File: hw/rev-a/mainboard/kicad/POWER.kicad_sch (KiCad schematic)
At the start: 66 parts, among them J10 5V PWR, J11 9V POWER, J13 9V POWER JACK, J27 6V POWER, J8 PET POWER, U3 AMS1117-3.3, U4 LM317AG-TN3-R, U5 LM317AG-TN3-R, U6 TPS5430DDA

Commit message: hw: use TLV1117LV instead of AMS1117
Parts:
- C89: value 15000u -> 120uF; MOUSER 661-BV250L153AM40S -> 667-EEU-FM1H121LB; now fitted
- R6, R8: value 1 -> 0; LCSC C22936 -> C21189
- U3: value AMS1117-3.3 -> TLV1117LV33; LCSC C6186 -> C15578
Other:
- note added: "*TLV1117LV33 substituted for AMS1117-3.3 due to incorrect placement of R6/R8 for ESR compensation"
- note added: "Configurable PS filtering caps"
- note removed: "Optional PS filtering caps. Typically not populated."
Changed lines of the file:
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@@
 	(polyline
 		(pts
-			(xy 53.34 27.94) (xy 53.34 48.26)
+			(xy 53.34 30.48) (xy 53.34 48.26)
 		)
 		(stroke
@@
 	(polyline
 		(pts
-			(xy 86.36 48.26) (xy 86.36 27.94)
+			(xy 86.36 48.26) (xy 86.36 30.48)
 		)
 		(stroke
@@
 	(polyline
 		(pts
-			(xy 86.36 27.94) (xy 53.34 27.94)
+			(xy 86.36 30.48) (xy 53.34 30.48)
 		)
 		(stroke
@@
 		)
 	)
+	(text "*TLV1117LV33 substituted\nfor AMS1117-3.3 due to\nincorrect placement of\nR6/R8 for ESR compensation"
+		(exclude_from_sim no)
+		(at 127 190.5 0)
+		(effects
+			(font
+				(size 1.27 1.27)
+			)
+			(justify left)
+		)
+	)
 	(text "LM317A:\nΔV_{OUT}=~3V (at ≥ 10ma)\nUse 120R load resistor\n\nT8/T20Q144 Power Requirements\nAbsolute max VCORE: 1.42V\nTypical: 1.15V ~ 1.25V"
 		(exclude_from_sim no)
@@
 		)
 	)
-	(text "Optional PS filtering caps.\nTypically not populated."
+	(text "Configurable PS filtering caps"
 		(exclude_from_sim no)
 		(at 54.61 34.29 0)
@@
 			)
 		)
-		(property "Value" "1"
+		(property "Value" "0"
 			(at 120.65 177.292 90)
 			(effects
@@
 			)
 		)
-		(property "Datasheet" "https://www.lcsc.com/datasheet/lcsc_datasheet_2206010130_UNI-ROYAL-Uniroyal-Elec-0603WAF1004T5E_C22935.pdf"
+		(property "Datasheet" "https://jlcpcb.com/api/file/downloadByFileSystemAccessId/8578255895094087680"
 			(at 120.65 177.8 0)
 			(effects
@@
 			)
 		)
-		(property "LCSC" "C22936"
+		(property "LCSC" "C21189"
 			(at 120.65 177.8 0)
 			(effects
@@
 			)
 		)
-		(property "Value" "AMS1117-3.3"
+		(property "Value" "TLV1117LV33"
 			(at 114.3 161.29 0)
 			(effects
@@
 			)
 		)
-		(property "Datasheet" "https://jlcpcb.com/api/file/downloadByFileSystemAccessId/8550724073479806976"
+		(property "Datasheet" "https://www.ti.com/cn/lit/gpn/tlv1117lv"
 			(at 116.84 172.72 0)
 			(effects
@@
 			)
 		)
-		(property "LCSC" "C6186"
+		(property "LCSC" "C15578"
 			(at 114.3 166.37 0)
 			(effects
@@
 			)
 		)
-		(property "Value" "1"
+		(property "Value" "0"
 			(at 125.73 177.292 90)
 			(effects
@@
 			)
 		)
-		(property "Datasheet" "https://www.lcsc.com/datasheet/lcsc_datasheet_2206010130_UNI-ROYAL-Uniroyal-Elec-0603WAF1004T5E_C22935.pdf"
+		(property "Datasheet" "https://jlcpcb.com/api/file/downloadByFileSystemAccessId/8578255895094087680"
 			(at 125.73 177.8 0)
 			(effects
@@
 			)
 		)
-		(property "LCSC" "C22936"
+		(property "LCSC" "C21189"
 			(at 125.73 177.8 0)
 			(effects
@@
 		(in_bom yes)
 		(on_board yes)
-		(dnp yes)
+		(dnp no)
 		(property "Reference" "C89"
 			(at 61.9252 40.7416 0)
@@
 			)
 		)
-		(property "Value" "15000u"
+		(property "Value" "120uF"
 			(at 61.9252 43.053 0)
 			(effects
@@
 			)
 		)
-		(property "Datasheet" "https://www.chemi-con.co.jp/products/relatedfiles/capacitor/catalog/LBVLL-e.PDF"
+		(property "Datasheet" "https://industrial.panasonic.com/cdbs/www-data/pdf/RDF0000/ABA0000C1018.pdf"
 			(at 59.69 41.91 0)
 			(effects
@@
 			)
 		)
-		(property "Description" ""
+		(property "Description" "120uF 50V low-ESR capacitor"
 			(at 59.69 41.91 0)
 			(effects
@@
 			)
 		)
-		(property "MOUSER" "661-BV250L153AM40S"
+		(property "MOUSER" "667-EEU-FM1H121LB"
 			(at 59.69 41.91 0)
 			(effects

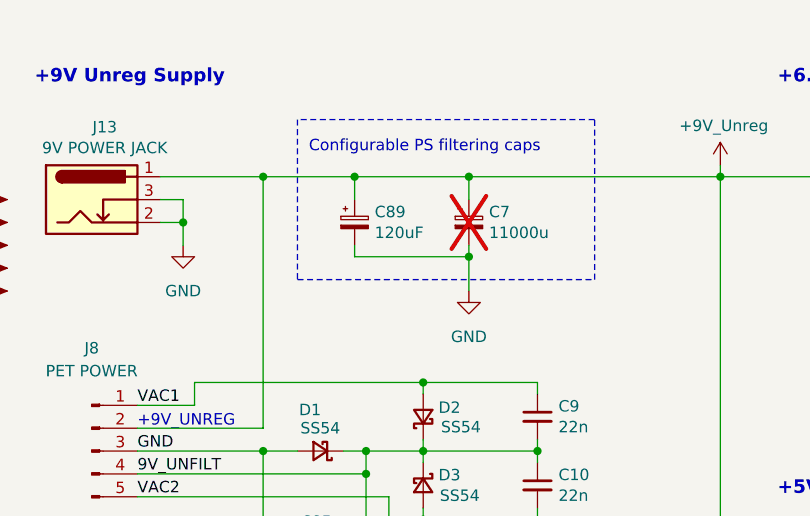
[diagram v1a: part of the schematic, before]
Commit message: hw: increase C89 to 330uF
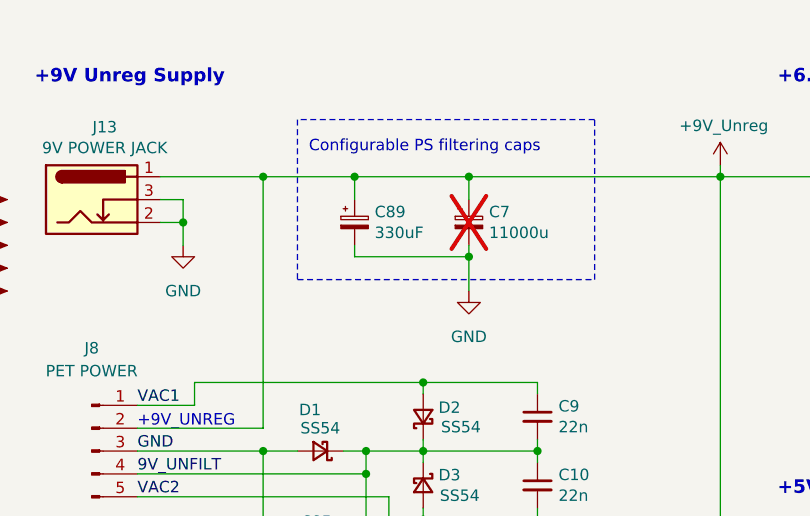
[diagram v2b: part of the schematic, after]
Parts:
- C89: value 120uF -> 330uF; MOUSER 667-EEU-FM1H121LB -> 667-EEU-FM1V331
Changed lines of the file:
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@@
 			)
 		)
-		(property "Value" "120uF"
+		(property "Value" "330uF"
 			(at 61.9252 43.053 0)
 			(effects
@@
 			)
 		)
-		(property "Description" "120uF 50V low-ESR capacitor"
+		(property "Description" "330uF 35V low-ESR capacitor"
 			(at 59.69 41.91 0)
 			(effects
@@
 			)
 		)
-		(property "MOUSER" "667-EEU-FM1H121LB"
+		(property "MOUSER" "667-EEU-FM1V331"
 			(at 59.69 41.91 0)
 			(effects

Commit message: hw: add notes to schematics
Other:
- note added: "18.3 VAC C.T. arrives on pins 1/5. Rectified DC leaves on pin 4, is externally smoothed by a 17-23mF capacitor and returns on pin 2. Despite being labeled 9V_UNREG in the CBM schematics, the actual voltage is closer to 12V. Pins 8/9 are not used by the replacement board. The PET power supply delivers 17 VAC on pins 8/9, which was used by the original mainboard to produce +16V DC for internal acce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"
- note added: "6.1V @ ~700ma max (~350ma per cassette port) Voltage and limits derived from PET schematics and datasheets Voltage is non-critical as the datasette speed is controlled by a mechanical governor. Heatsink does not appear to be required for a single Datasette. (Running two Datasettes at the same time hasn't been tested.)"
- note removed: "18.3 VAC C.T. arrives on pins 1/5. Rectified +9V DC leaves on pin 4, is externally connected to a 23000u capacitor to reduce ripple, and returns on pin 2. Pins 8/9 are not used by the replacement board. The PET power supply delivers 17 VAC on pins 8/9, which was used by the original mainboard to produce +16V DC for internal accessories. The CRT gets power directly from the transformer. Capactiors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"
- note removed: "6.1V @ ~700ma max (~350ma per cassette port) Voltage and limits derived from PET schematics and datasheets Voltage is non-critical as the datasette speed is controlled by a mechanical governor. Heatsink does not appear to be required."
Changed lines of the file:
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@@
 		)
 	)
-	(text "18.3 VAC C.T. arrives on pins 1/5.\n\nRectified +9V DC leaves on pin 4, is externally\nconnected to a 23000u capacitor to reduce ripple,\nand returns on pin 2.\n\nPins 8/9 are not used by the replacement board.\nThe PET power supply delivers 17 VAC on pins 8/9,\nwhich was used by the original mainboard to\nproduce +16V DC for internal accessories.\n\nThe CRT gets power directly from the transformer.\n\nCapactiors must be derated by ~30% for AC:\n9V AC * 1.415 = ~13V DC"
+	(text "18.3 VAC C.T. arrives on pins 1/5. Rectified DC\nleaves on pin 4, is externally smoothed by a\n17-23mF capacitor and returns on pin 2.\n\nDespite being labeled 9V_UNREG in the CBM\nschematics, the actual voltage is closer to 12V.\n\nPins 8/9 are not used by the replacement board.\nThe PET power supply delivers 17 VAC on pins 8/9,\nwhich was used by the original mainboard to\nproduce +16V DC for internal accessories.\n\nThe CRT gets power directly from the transformer.\n\nCapactiors must be derated by ~30% for AC:\n12V AC * 1.415 = ~17V DC\n\nUse min 25V for caps connected to +9V_UNREG"
 		(exclude_from_sim no)
-		(at 21.59 121.92 0)
+		(at 29.21 132.08 0)
 		(effects
 			(font
@@
 		)
 	)
-	(text "6.1V @ ~700ma max\n(~350ma per cassette port)\n\nVoltage and limits derived from\nPET schematics and datasheets\n\nVoltage is non-critical as the\ndatasette speed is controlled by\na mechanical governor.\n\nHeatsink does not appear to be\nrequired."
+	(text "6.1V @ ~700ma max\n(~350ma per cassette port)\n\nVoltage and limits derived from\nPET schematics and datasheets\n\nVoltage is non-critical as the\ndatasette speed is controlled by\na mechanical governor.\n\nHeatsink does not appear to be\nrequired for a single Datasette.\n\n(Running two Datasettes at the\nsame time hasn't been tested.)\n"
 		(exclude_from_sim no)
-		(at 170.18 62.23 0)
+		(at 170.18 68.58 0)
 		(effects
 			(font
